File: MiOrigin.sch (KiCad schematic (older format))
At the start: 31 parts, among them J3 Micro_SD_Card, J5 DB9_Male_MountingHoles, Q1 PMBT3904YS, U1 ESP32-WROOM-32U, U4 3.5-TFT-LCD-SPI, U7 SN74LVC125ADBR_(Units), U8 MAX3232

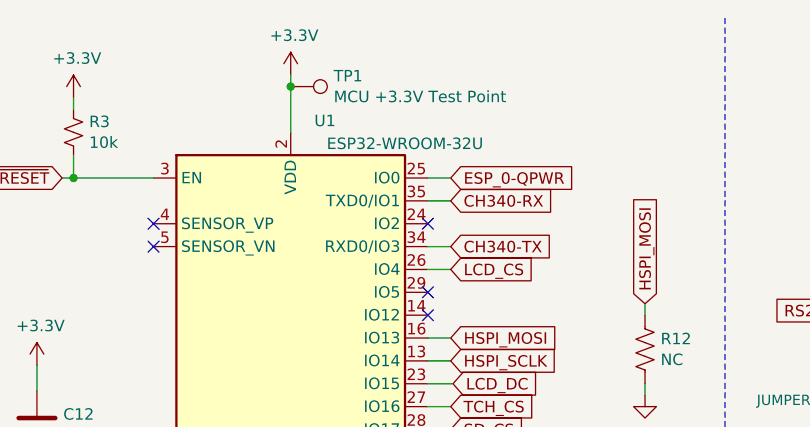
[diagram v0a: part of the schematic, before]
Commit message: Replace USB to UART with CP2102-GM
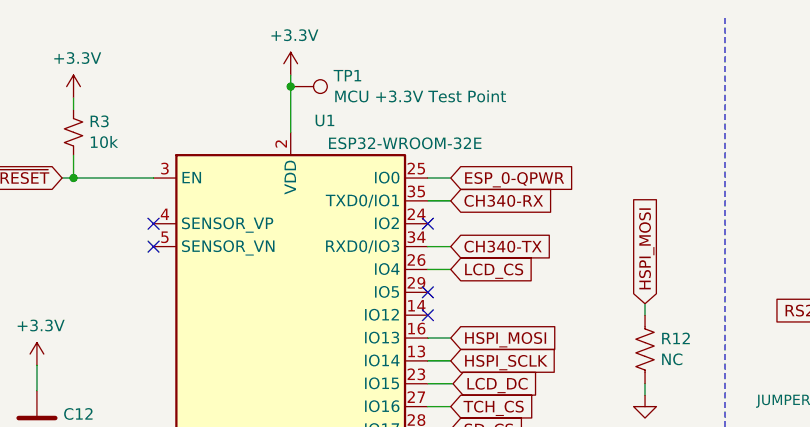
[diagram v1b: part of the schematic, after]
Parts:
- U1: value ESP32-WROOM-32U -> ESP32-WROOM-32E; DigiKey https://www.digikey.com/en/products/detail/espressif-systems/ESP32-WROOM-32E-4MB-HIGH-TEMP/12696413 -> https://www.digikey.com/en/products/detail/espressif-systems/ESP32-WROOM-32E-16MB/11613144; DigiKey(Alt) (none) -> https://www.digikey.com/en/products/detail/espressif-system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
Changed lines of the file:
@@
 P 1800 2350
 F 0 "U1" H 1950 3800 50  0000 C CNN
-F 1 "ESP32-WROOM-32U" H 2300 3700 50  0000 C CNN
+F 1 "ESP32-WROOM-32E" H 2300 3700 50  0000 C CNN
 F 2 "RF_Module:ESP32-WROOM-32" H 1800 850 50  0001 C CNN
 F 3 "https://www.espressif.com/sites/default/files/documentation/esp32-wroom-32d_esp32-wroom-32u_datasheet_en.pdf" H 1500 2400 50  0001 C CNN
-F 4 "https://www.digikey.com/en/products/detail/espressif-systems/ESP32-WROOM-32E-4MB-HIGH-TEMP/12696413" H 1800 2350 50  0001 C CNN "DigiKey"
+F 4 "https://www.digikey.com/en/products/detail/espressif-systems/ESP32-WROOM-32E-16MB/11613144" H 1800 2350 50  0001 C CNN "DigiKey"
 F 5 "ESP32-WROOM-32E (4MB HIGH TEMP)" H 1800 2350 50  0001 C CNN "MPN"
+F 6 "https://www.digikey.com/en/products/detail/espressif-systems/ESP32-WROOM-32E-4MB-HIGH-TEMP/12696413" H 1800 2350 50  0001 C CNN "DigiKey(Alt)"
 	1    1800 2350
 	1    0    0    -1

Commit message: Update board
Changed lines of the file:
@@
 Wire Wire Line
 	9230 1780 9330 1780
-Text Notes 9690 1020 0    118  ~ 0
+Text Notes 9730 3685 0    118  ~ 0
 microSD Card
 Wire Notes Line
